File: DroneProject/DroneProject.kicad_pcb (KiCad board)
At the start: 4 copper layers, 50 x 100 mm, 106 parts, among them J21 Battery, J22 Debug, J23 UART, Q21 IRLML5203, SW1 PTS815 SJM 250 SMTR LFS, U31 AP63205WU, U32 TLV75533PDBV, U41 STM32F410RBT6, U61 LSM6DSOTR, U62 TMAG5273C1QDBVR, U63 INA181A1IDBVR, U64 M24C02-WMN6TP, Y41 LFXTAL003151

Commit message: Finished initial PCB layout.  However decided to go ahead and add the motor drivers for the first prototype anyways.  Re-did the reverse-polarity detection to use an NMOS instead of a PMOS.  Added sheets for each motor, still need to decide on parts.
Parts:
- added TP715: PWM2, Library:Testpoint 1.6mm x 0.8mm, F.Cu at (340.9, 72.7)
- added TP716: PWM3, Library:Testpoint 1.6mm x 0.8mm, F.Cu at (340.9, 74.5)
- added TP717: PWM4, Library:Testpoint 1.6mm x 0.8mm, F.Cu at (340.9, 76.3)
- C35, C36, C37, C38, C49, C51, C52, C53, C54, C61, C62, C63, C64, FB41, FB51, FB61, R21, R22, R41, R43, R44, R45, R46, R47, R48, R49, R51, R52, R53, R54, R61, R62, R63: moved to B.Cu
- moved R31 267.4 mm to (137.6, 59.8), turned to 90 degrees
- moved SW31 255.8 mm to (140.9, 64.0), turned to -90 degrees
- moved C39 254.5 mm to (136.4, 59.8), turned to 90 degrees
- moved C62 246.2 mm to (143.6, 111.3), turned to -90 degrees
- moved C610 245.9 mm to (137.5, 142.6), turned to -90 degrees
- moved R63 243.1 mm to (146.0, 109.3)
- moved C64 242.9 mm to (150.2, 104.3), turned to 90 degrees
- moved R62 242.8 mm to (146.0, 108.3)
- moved R61 238.9 mm to (150.2, 106.2), turned to 90 degrees
- moved U61 237.2 mm to (150.0, 108.6)
- moved C66 235.6 mm to (160.1, 101.3), turned to 180 degrees
- moved U63 234.8 mm to (142.3, 139.0), turned to -90 degrees
- moved FB61 233.4 mm to (147.3, 112.0), turned to 90 degrees
- moved C35 231.9 mm to (153.5, 121.2), turned to -90 degrees
- moved R64 231.5 mm to (158.3, 111.6), turned to 90 degrees
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- renumbered SW1 to SW31
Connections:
- net ISEN- renamed GND
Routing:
- net GND: track 0.00 -> 97.4 mm, vias 0 -> 33
- net NRST: track 0.00 -> 88.8 mm, vias 0 -> 4
- net +5V: track 0.00 -> 88.1 mm, vias 0 -> 5
- net +3.3V: track 0.00 -> 79.8 mm, vias 0 -> 13
- net SWO: track 0.00 -> 69.0 mm, vias 0 -> 1
- net ISEN_ADC: track 0.00 -> 59.4 mm, vias 0 -> 2
- net SWCLK: track 0.00 -> 57.1 mm, vias 0 -> 2
- net VBAT_TVS: track 0.00 -> 56.2 mm, vias 0 -> 1
- net MAG_INT: track 0.00 -> 51.4 mm, vias 0 -> 2
- net SWDIO: track 0.00 -> 44.9 mm
- net I2C1_SDA: track 0.00 -> 43.1 mm, vias 0 -> 5
- net I2C1_SCL: track 0.00 -> 42.5 mm, vias 0 -> 3
- net UART_RX: track 0.00 -> 40.5 mm, vias 0 -> 1
- net UART_TX: track 0.00 -> 39.4 mm, vias 0 -> 2
- net EEPROM_WC: track 0.00 -> 38.5 mm, vias 0 -> 4
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- added copper zone on In2.Cu, net +3.3V
- added copper zone on In2.Cu, net +5V
- added copper zone on In1.Cu, net GND
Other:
- board text added: "3.3V"
- board text added: "3P3"
- board text added: "5"
- board text added: "5V"
- board text added: "GND"
- board text added: "I2C1_SCL"
- board text added: "I2C1_SDA"
- board text added: "IMU_CSN"
- board text added: "NRST"
- board text added: "PWR_GOOD"
- board text added: "RESET"
- board text added: "RX"
- board text added: "SPI1_MISO"
- board text added: "SPI1_MOSI"
- board text added: "SPI1_SCK"
- board text added: "SPI2_MISO"
- board text added: "SPI2_MOSI"
- board text added: "SPI2_SCK"
- board text added: "STATUS"
- board text added: "SWCLK"
- board text added: "SWDIO"
- board text added: "SWO"
- board text added: "TR_CSN"
- board text added: "TX"

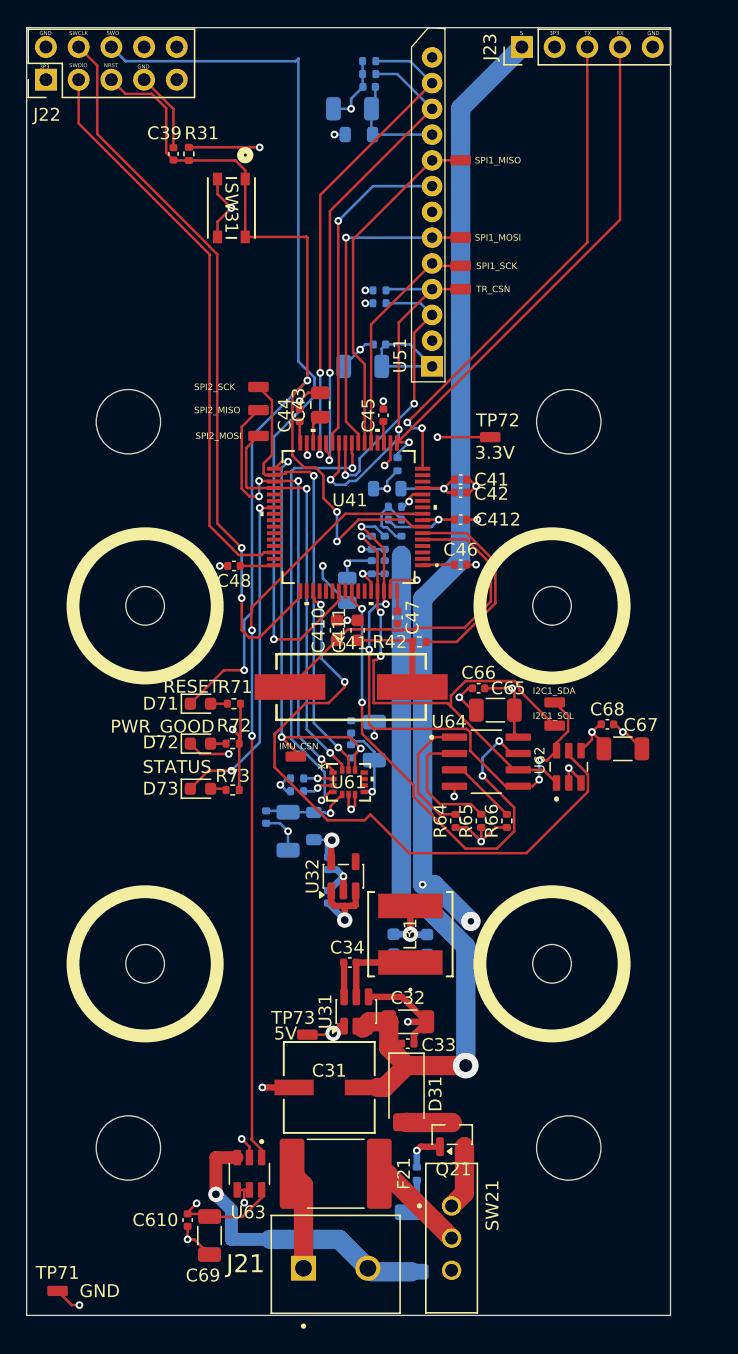
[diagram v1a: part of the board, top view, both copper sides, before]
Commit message: Re-did layout for new power system
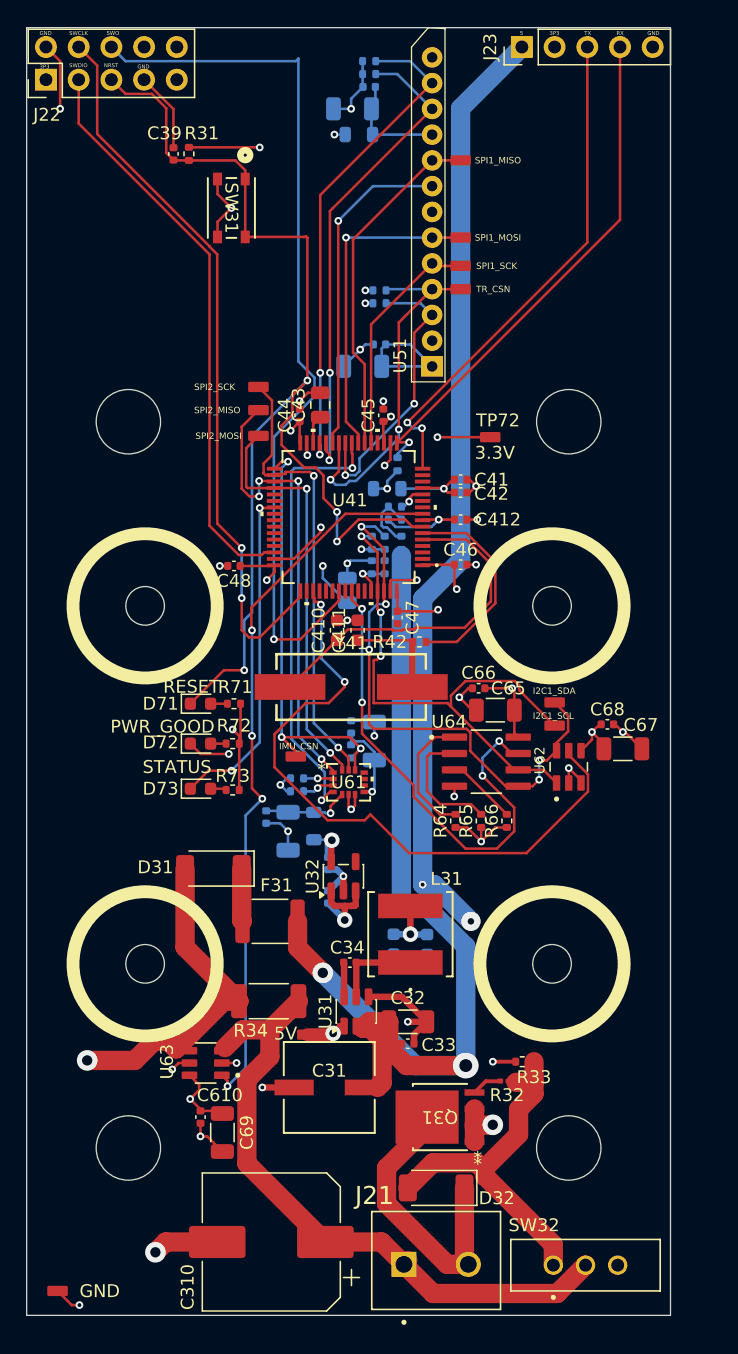
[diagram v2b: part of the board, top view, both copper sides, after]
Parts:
- removed F21: Fuse, Fuse:Fuse_2920_7451Metric
- removed Q21: IRLML5203, Package_TO_SOT_SMD:SOT-23
- removed R21: 100K, Resistor_SMD:R_0402_1005Metric
- removed R22: 5m, Resistor_SMD:R_2010_5025Metric
- removed SW21: ~, Library:SW_EG1218
- added C310: 470uF, Capacitor_SMD:CP_Elec_10x10.5, F.Cu at (144.0, 144.3)
- added D32: SM6F14AY, Diode_SMD:D_SOD-128, F.Cu at (156.8, 140.1)
- added F31: Fuse 1A, Fuse:Fuse_1812_4532Metric, F.Cu at (143.9, 119.4)
- added Q31: RJK0654DPB-00-J5, Library:LFPAK_REN, F.Cu at (157.1, 134.6)
- added R32: 100, Resistor_SMD:R_0201_0603Metric, F.Cu at (162.1, 131.8)
- added R33: 100K, Resistor_SMD:R_0402_1005Metric, F.Cu at (163.5, 130.3)
- added R34: Shunt, Resistor_SMD:R_2010_5025Metric, F.Cu at (143.8, 125.6)
- added SW32: ~, Library:SW_EG1218, F.Cu at (168.4, 146.1)
- moved D31 23.0 mm to (139.5, 115.3), turned to 180 degrees
- moved U63 9.25 mm to (138.9, 130.4), turned to 180 degrees
- moved C610 8.06 mm to (138.5, 134.6)
- moved C69 8.06 mm to (140.2, 135.8)
- moved J21 7.81 mm to (154.3, 146.0)
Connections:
- D31 pad 1: VBAT_TVS -> Net-(D31-K)
- D31 pad 2: VBAT_PROT -> VDD
- J21 pad 2: ISEN+ -> -BATT
- U63 pad 3: ISEN+ -> +BATT
- U63 pad 4: GND -> VDD
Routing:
- net +BATT: track 7.71 -> 50.1 mm
- net /Power/VBAT_SW: track 0.00 -> 28.4 mm
- net VDD: track 0.00 -> 26.2 mm, vias 0 -> 1
- net ISEN+: track 23.5 -> 0.00 mm, vias 1 -> 0
- net -BATT: track 0.00 -> 23.3 mm
- net VBAT_TVS: track 56.2 -> 77.8 mm, vias 1 -> 2
- net GND: track 97.4 -> 114.8 mm, vias 33 -> 38
- net /Connectors/VBAT_FUSE: track 7.68 -> 0.00 mm
- net +3.3V: track 79.8 -> 85.5 mm, vias 13 -> 18
- net /Connectors/VBAT_SW: track 5.01 -> 0.00 mm
- net Net-(D31-K): track 0.00 -> 4.13 mm
- net VBAT_PROT: track 3.56 -> 0.00 mm
- net ISEN_ADC: track 59.4 -> 56.0 mm, vias 2 -> 4
- net /Connectors/VBAT_MOS_GATE: track 3.21 -> 0.00 mm, vias 1 -> 0
- net /Power/VBAT_SW_R: track 0.00 -> 2.28 mm
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- added copper zone on In2.Cu, net VDD

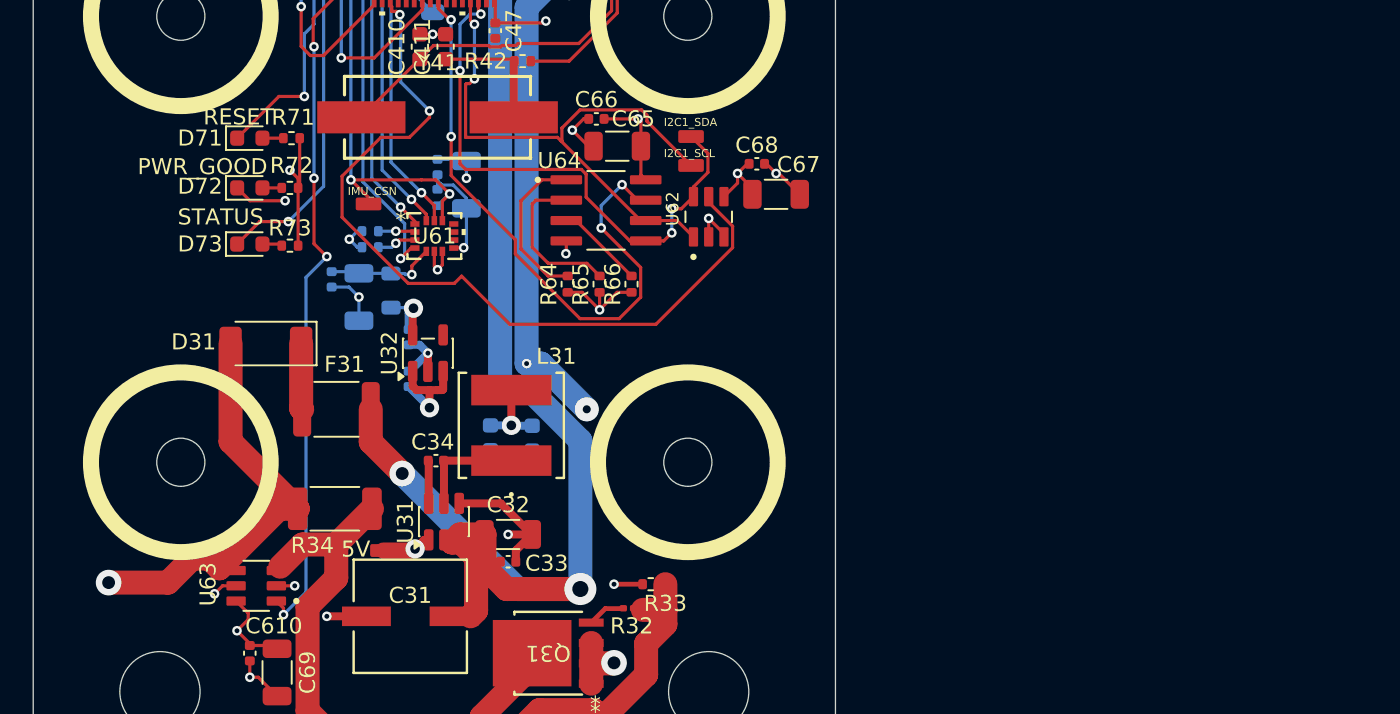
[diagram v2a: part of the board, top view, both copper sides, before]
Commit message: Added a second MCU for motor control.  Removed 5V rail.  Added COM switching for SWD and UART external headers
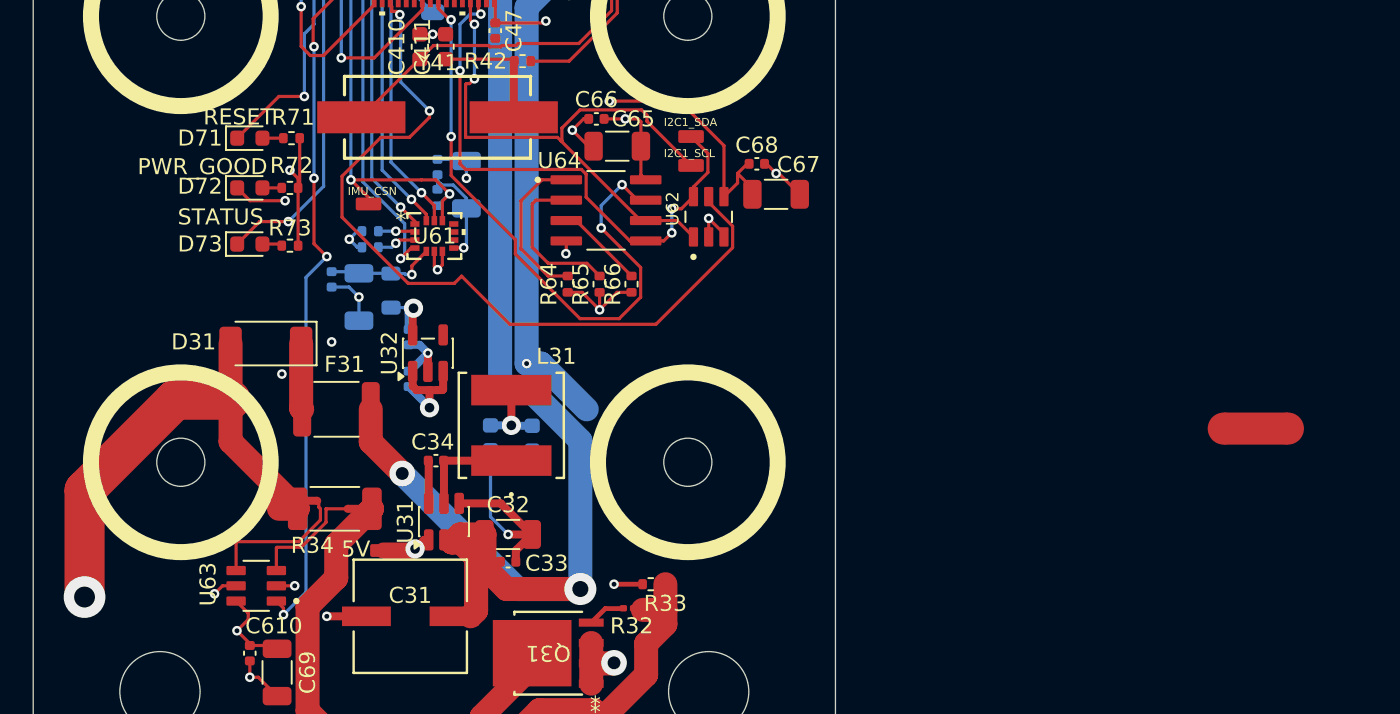
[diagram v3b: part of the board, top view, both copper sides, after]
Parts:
- added NT31: NetTie_2, NetTie:NetTie-2_SMD_Pad0.5mm, F.Cu at (145.1, 125.6)
- added NT32: NetTie_2, NetTie:NetTie-2_SMD_Pad0.5mm, F.Cu at (142.2, 125.1)
- added NT33: NetTie_2, NetTie:NetTie-2_SMD_Pad2.0mm, F.Cu at (201.2, 120.6)
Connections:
- U63 pad 3: +BATT -> ISENSE+
- U63 pad 4: VDD -> ISENSE-
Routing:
- net +3.3V: track 85.5 -> 97.0 mm, vias 18 -> 19
- net ISENSE-: track 0.00 -> 8.86 mm
- net GND: track 114.8 -> 123.3 mm, vias 38 -> 39
- net ISENSE+: track 0.00 -> 7.36 mm
- net VDD: track 26.2 -> 31.3 mm
- net +BATT: track 50.1 -> 46.4 mm
- net +5V: vias 5 -> 4

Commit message: Finished most of routing for motor controls, however likely going to revert back and make separate ESC boards for motor control as I think that would honestly be more efficient from both a cost and debug complexity standpoint.
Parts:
- removed C310: 470uF, Capacitor_SMD:CP_Elec_10x10.5
- removed C39: 0.1uF, Capacitor_SMD:C_0402_1005Metric
- removed C410, C411: 27pF, Capacitor_SMD:C_0603_1608Metric
- removed R42: 0, Resistor_SMD:R_0402_1005Metric
- removed TP714: PWM1, Library:Testpoint 1.6mm x 0.8mm
- removed TP715: PWM2, Library:Testpoint 1.6mm x 0.8mm
- removed TP716: PWM3, Library:Testpoint 1.6mm x 0.8mm
- removed TP717: PWM4, Library:Testpoint 1.6mm x 0.8mm
- removed TP73: POS5, Library:Testpoint 1.6mm x 0.8mm
- removed U32: TLV75533PDBV, Package_TO_SOT_SMD:SOT-23-5
- removed Y41: LFXTAL003151, Library:WE-XTAL_HC49_4HSMX
- added C101: 10uF, Capacitor_SMD:C_1206_3216Metric, F.Cu at (130.5, 114.5)
- added C1010: 1uF, Capacitor_SMD:C_0603_1608Metric, F.Cu at (109.3, 133.6)
- added C1011: 0.1uF, Capacitor_SMD:C_0402_1005Metric, B.Cu at (127.1, 121.6)
- added C1012: 1uF, Capacitor_SMD:C_0603_1608Metric, F.Cu at (112.4, 126.1)
- added C1013: 1uF, Capacitor_SMD:C_0603_1608Metric, F.Cu at (109.3, 126.1)
- added C1014: 1uF, Capacitor_SMD:C_0603_1608Metric, F.Cu at (112.3, 118.5)
- added C1015: 1uF, Capacitor_SMD:C_0603_1608Metric, F.Cu at (109.3, 118.5)
- added C102: 0.1uF, Capacitor_SMD:C_0402_1005Metric, F.Cu at (128.8, 115.8)
- added C103: 1uF, Capacitor_SMD:C_0402_1005Metric, F.Cu at (127.8, 115.8)
- added C104: 47nF, Capacitor_SMD:C_0402_1005Metric, F.Cu at (126.4, 113.4)
- added C105: 1uF, Capacitor_SMD:C_0402_1005Metric, B.Cu at (118.4, 115.5)
- added C106: 440uF, Capacitor_THT:CP_Radial_D10.0mm_P5.00mm, F.Cu at (115.6, 142.0)
- added C108: 0.1uF, Capacitor_SMD:C_0402_1005Metric, B.Cu at (127.1, 129.1)
- added C109: 1uF, Capacitor_SMD:C_0603_1608Metric, F.Cu at (112.4, 133.6)
- added C111: 10uF, Capacitor_SMD:C_1206_3216Metric, F.Cu at (175.5, 100.3)
- added C1110: 1uF, Capacitor_SMD:C_0603_1608Metric, F.Cu at (191.1, 92.7)
- added C1111: 0.1uF, Capacitor_SMD:C_0402_1005Metric, B.Cu at (173.0, 91.8)
- added C1112: 1uF, Capacitor_SMD:C_0603_1608Metric, F.Cu at (188.4, 85.2)
- added C1113: 1uF, Capacitor_SMD:C_0603_1608Metric, F.Cu at (191.4, 85.2)
- added C1114: 1uF, Capacitor_SMD:C_0603_1608Metric, F.Cu at (188.4, 77.5)
- added C1115: 1uF, Capacitor_SMD:C_0603_1608Metric, F.Cu at (191.4, 77.5)
- added C112: 0.1uF, Capacitor_SMD:C_0402_1005Metric, F.Cu at (177.2, 99.0)
- added C113: 1uF, Capacitor_SMD:C_0402_1005Metric, F.Cu at (178.2, 99.0)
- added C114: 47nF, Capacitor_SMD:C_0402_1005Metric, F.Cu at (177.7, 101.5)
- added C115: 1uF, Capacitor_SMD:C_0402_1005Metric, B.Cu at (187.6, 99.7)
- added C116: 440uF, Capacitor_THT:CP_Radial_D10.0mm_P5.00mm, F.Cu at (197.4, 102.0)
- added C118: 0.1uF, Capacitor_SMD:C_0402_1005Metric, B.Cu at (172.8, 84.3)
- added C119: 1uF, Capacitor_SMD:C_0603_1608Metric, F.Cu at (188.0, 92.7)
- added C121: 10uF, Capacitor_SMD:C_1206_3216Metric, F.Cu at (112.0, 96.8)
- added C1210: 1uF, Capacitor_SMD:C_0603_1608Metric, F.Cu at (108.5, 92.7)
- added C1211: 0.1uF, Capacitor_SMD:C_0402_1005Metric, B.Cu at (127.0, 77.9)
- added C1212: 1uF, Capacitor_SMD:C_0603_1608Metric, F.Cu at (111.6, 85.1)
- added C1213: 1uF, Capacitor_SMD:C_0603_1608Metric, F.Cu at (108.5, 85.1)
- added C1214: 1uF, Capacitor_SMD:C_0603_1608Metric, F.Cu at (111.7, 77.5)
- added C1215: 1uF, Capacitor_SMD:C_0603_1608Metric, F.Cu at (108.7, 77.5)
- added C122: 0.1uF, Capacitor_SMD:C_0402_1005Metric, F.Cu at (113.7, 98.1)
- added C123: 1uF, Capacitor_SMD:C_0402_1005Metric, F.Cu at (114.7, 99.1)
- added C124: 47nF, Capacitor_SMD:C_0402_1005Metric, F.Cu at (114.2, 101.4)
- added C125: 1uF, Capacitor_SMD:C_0402_1005Metric, B.Cu at (123.3, 99.7)
- added C126: 440uF, Capacitor_THT:CP_Radial_D10.0mm_P5.00mm, F.Cu at (102.6, 102.0)
- added C128: 0.1uF, Capacitor_SMD:C_0402_1005Metric, B.Cu at (127.1, 85.5)
- added C129: 1uF, Capacitor_SMD:C_0603_1608Metric, F.Cu at (111.5, 92.7)
- added C131: 0.1uF, Capacitor_SMD:C_0402_1005Metric, F.Cu at (139.2, 64.0)
- added C133: 0.1uF, Capacitor_SMD:C_0402_1005Metric, F.Cu at (130.6, 64.0)
- added C134: 0.1uF, Capacitor_SMD:C_0402_1005Metric, F.Cu at (180.6, 58.3)
- added C81: 4.7uF, Capacitor_SMD:C_0805_2012Metric, B.Cu at (161.3, 109.0)
- added C810: 1nf, Capacitor_SMD:C_0402_1005Metric, B.Cu at (140.0, 101.8)
- added C811: 1nf, Capacitor_SMD:C_0402_1005Metric, B.Cu at (135.0, 102.9)
- added C812: 1nf, Capacitor_SMD:C_0402_1005Metric, B.Cu at (135.0, 100.9)
- added C813: 1uF, Capacitor_SMD:C_0402_1005Metric, B.Cu at (149.1, 92.5)
- added C814: 0.1uF, Capacitor_SMD:C_0402_1005Metric, B.Cu at (150.1, 92.5)
- added C815: 1nf, Capacitor_SMD:C_0402_1005Metric, B.Cu at (145.6, 89.7)
- added C816: 1nf, Capacitor_SMD:C_0402_1005Metric, B.Cu at (147.6, 89.7)
- added C817: 1nf, Capacitor_SMD:C_0402_1005Metric, B.Cu at (149.6, 89.8)
- added C818: 1nf, Capacitor_SMD:C_0402_1005Metric, B.Cu at (151.6, 89.8)
- added C82: 0.1uF, Capacitor_SMD:C_0402_1005Metric, B.Cu at (156.8, 96.1)
- added C83: 0.1uF, Capacitor_SMD:C_0402_1005Metric, B.Cu at (160.5, 107.5)
- added C84: 0.1uF, Capacitor_SMD:C_0402_1005Metric, B.Cu at (140.1, 108.3)
- added C85: 0.1uF, Capacitor_SMD:C_0402_1005Metric, B.Cu at (146.6, 114.1)
- added C86: 0.1uF, Capacitor_SMD:C_0402_1005Metric, B.Cu at (140.1, 99.2)
- added C87: 1uF, Capacitor_SMD:C_0402_1005Metric, B.Cu at (154.4, 95.0)
- added C88: 10nF, Capacitor_SMD:C_0402_1005Metric, B.Cu at (155.4, 95.0)
- added C89: 1nf, Capacitor_SMD:C_0402_1005Metric, B.Cu at (140.0, 105.0)
- added C91: 10uF, Capacitor_SMD:C_1206_3216Metric, F.Cu at (183.3, 117.1)
- added C910: 1uF, Capacitor_SMD:C_0603_1608Metric, F.Cu at (191.9, 133.8)
- added C911: 0.1uF, Capacitor_SMD:C_0402_1005Metric, B.Cu at (172.8, 129.2)
- added C912: 1uF, Capacitor_SMD:C_0603_1608Metric, F.Cu at (188.8, 126.4)
- added C913: 1uF, Capacitor_SMD:C_0603_1608Metric, F.Cu at (191.9, 126.4)
- added C914: 1uF, Capacitor_SMD:C_0603_1608Metric, F.Cu at (188.9, 118.4)
- added C915: 1uF, Capacitor_SMD:C_0603_1608Metric, F.Cu at (191.9, 118.4)
- added C92: 0.1uF, Capacitor_SMD:C_0402_1005Metric, F.Cu at (181.6, 115.8)
- added C93: 1uF, Capacitor_SMD:C_0402_1005Metric, F.Cu at (180.6, 115.8)
- added C94: 47nF, Capacitor_SMD:C_0402_1005Metric, F.Cu at (179.2, 113.4)
- added C95: 1uF, Capacitor_SMD:C_0402_1005Metric, B.Cu at (171.2, 114.5)
- added C96: 440uF, Capacitor_THT:CP_Radial_D10.0mm_P5.00mm, F.Cu at (184.4, 142.0)
- added C98: 0.1uF, Capacitor_SMD:C_0402_1005Metric, B.Cu at (172.7, 134.5)
- added C99: 1uF, Capacitor_SMD:C_0603_1608Metric, F.Cu at (188.8, 133.8)
- added D131: C1, LED_SMD:LED_0603_1608Metric, F.Cu at (169.6, 62.8)
- added D132: C0, LED_SMD:LED_0603_1608Metric, F.Cu at (167.9, 62.8)
- added FB81: FerriteBead, Inductor_SMD:L_0805_2012Metric, B.Cu at (152.3, 94.2)
- added J24: Screw_Terminal_01x03, Library:CUI_TB005_-762-03BE, F.Cu at (198.4, 130.2)
- added J25: Screw_Terminal_01x03, Library:CUI_TB005_-762-03BE, F.Cu at (101.7, 114.9)
- added J26: Screw_Terminal_01x03, Library:CUI_TB005_-762-03BE, F.Cu at (198.4, 89.1)
- added J27: Screw_Terminal_01x03, Library:CUI_TB005_-762-03BE, F.Cu at (101.6, 73.9)
- added NT10: NetTie_2, NetTie:NetTie-2_SMD_Pad0.5mm, B.Cu at (123.5, 88.2)
- added NT101: NetTie_2, NetTie:NetTie-2_SMD_Pad0.5mm, B.Cu at (118.9, 130.9)
- added NT102: NetTie_2, NetTie:NetTie-2_SMD_Pad0.5mm, B.Cu at (118.9, 123.4)
- added NT111: NetTie_2, NetTie:NetTie-2_SMD_Pad0.5mm, B.Cu at (181.2, 90.0)
- added NT112: NetTie_2, NetTie:NetTie-2_SMD_Pad0.5mm, B.Cu at (181.0, 82.5)
- added NT12: NetTie_2, NetTie:NetTie-2_SMD_Pad0.5mm, B.Cu at (123.5, 80.6)
- added NT121: NetTie_2, NetTie:NetTie-2_SMD_Pad0.5mm, B.Cu at (119.0, 88.2)
- added NT122: NetTie_2, NetTie:NetTie-2_SMD_Pad0.5mm, B.Cu at (119.0, 80.6)
- added NT2: NetTie_2, NetTie:NetTie-2_SMD_Pad0.5mm, B.Cu at (123.6, 130.9)
- added NT4: NetTie_2, NetTie:NetTie-2_SMD_Pad0.5mm, B.Cu at (123.6, 123.4)
- added NT6: NetTie_2, NetTie:NetTie-2_SMD_Pad0.5mm, B.Cu at (176.5, 90.0)
- added NT8: NetTie_2, NetTie:NetTie-2_SMD_Pad0.5mm, B.Cu at (176.3, 82.5)
- added NT91: NetTie_2, NetTie:NetTie-2_SMD_Pad0.5mm, B.Cu at (181.1, 132.4)
- added NT92: NetTie_2, NetTie:NetTie-2_SMD_Pad0.5mm, B.Cu at (176.4, 132.4)
- added NT93: NetTie_2, NetTie:NetTie-2_SMD_Pad0.5mm, B.Cu at (180.9, 127.0)
- added NT94: NetTie_2, NetTie:NetTie-2_SMD_Pad0.5mm, B.Cu at (176.4, 127.0)
- added Q101: CSD17577Q5A, Package_TO_SOT_SMD:TDSON-8-1, F.Cu at (110.3, 130.0)
- added Q102: CSD17577Q5A, Package_TO_SOT_SMD:TDSON-8-1, B.Cu at (113.8, 130.0)
- added Q103: CSD17577Q5A, Package_TO_SOT_SMD:TDSON-8-1, F.Cu at (110.3, 122.5)
- added Q104: CSD17577Q5A, Package_TO_SOT_SMD:TDSON-8-1, B.Cu at (113.8, 122.5)
- added Q105: CSD17577Q5A, Package_TO_SOT_SMD:TDSON-8-1, F.Cu at (110.3, 114.8)
- added Q106: CSD17577Q5A, Package_TO_SOT_SMD:TDSON-8-1, B.Cu at (113.8, 114.8)
- added Q111: CSD17577Q5A, Package_TO_SOT_SMD:TDSON-8-1, F.Cu at (189.8, 89.1)
- added Q112: CSD17577Q5A, Package_TO_SOT_SMD:TDSON-8-1, B.Cu at (186.3, 89.1)
- added Q113: CSD17577Q5A, Package_TO_SOT_SMD:TDSON-8-1, F.Cu at (189.8, 81.5)
- added Q114: CSD17577Q5A, Package_TO_SOT_SMD:TDSON-8-1, B.Cu at (186.2, 81.5)
- added Q115: CSD17577Q5A, Package_TO_SOT_SMD:TDSON-8-1, F.Cu at (189.8, 73.9)
- added Q116: CSD17577Q5A, Package_TO_SOT_SMD:TDSON-8-1, B.Cu at (186.3, 73.9)
- added Q121: CSD17577Q5A, Package_TO_SOT_SMD:TDSON-8-1, F.Cu at (110.2, 89.1)
- added Q122: CSD17577Q5A, Package_TO_SOT_SMD:TDSON-8-1, B.Cu at (113.8, 89.1)
- added Q123: CSD17577Q5A, Package_TO_SOT_SMD:TDSON-8-1, F.Cu at (110.2, 81.5)
- added Q124: CSD17577Q5A, Package_TO_SOT_SMD:TDSON-8-1, B.Cu at (113.7, 81.5)
- added Q125: CSD17577Q5A, Package_TO_SOT_SMD:TDSON-8-1, F.Cu at (110.2, 73.8)
- added Q126: CSD17577Q5A, Package_TO_SOT_SMD:TDSON-8-1, B.Cu at (113.7, 73.8)
- added Q91: CSD17577Q5A, Package_TO_SOT_SMD:TDSON-8-1, F.Cu at (189.8, 130.2)
- added Q92: CSD17577Q5A, Package_TO_SOT_SMD:TDSON-8-1, B.Cu at (186.2, 130.2)
- added Q93: CSD17577Q5A, Package_TO_SOT_SMD:TDSON-8-1, F.Cu at (189.8, 122.7)
- added Q94: CSD17577Q5A, Package_TO_SOT_SMD:TDSON-8-1, B.Cu at (186.2, 122.7)
- added Q95: CSD17577Q5A, Package_TO_SOT_SMD:TDSON-8-1, F.Cu at (189.8, 114.9)
- added Q96: CSD17577Q5A, Package_TO_SOT_SMD:TDSON-8-1, B.Cu at (186.2, 114.9)
- added R101: 10K, Resistor_SMD:R_0402_1005Metric, B.Cu at (118.4, 116.5)
- added R102: 10K, Resistor_SMD:R_0402_1005Metric, B.Cu at (122.1, 112.1)
- added R103: 10K, Resistor_SMD:R_0402_1005Metric, B.Cu at (123.1, 112.1)
- added R104: 10K, Resistor_SMD:R_0402_1005Metric, B.Cu at (124.1, 112.1)
- added R105: 10K, Resistor_SMD:R_0402_1005Metric, B.Cu at (118.4, 119.5)
- added R106: 33, Resistor_SMD:R_0402_1005Metric, B.Cu at (118.4, 118.5)
- added R107: 10K, Resistor_SMD:R_0402_1005Metric, B.Cu at (118.4, 117.5)
- added R108: CSS2H-2512K-2L00J, Resistor_SMD:R_2512_6332Metric, B.Cu at (121.2, 130.9)
- added R109: CSS2H-2512K-2L00J, Resistor_SMD:R_2512_6332Metric, B.Cu at (121.2, 123.4)
- added R111: 10K, Resistor_SMD:R_0402_1005Metric, B.Cu at (187.5, 98.7)
- added R112: 10K, Resistor_SMD:R_0402_1005Metric, B.Cu at (183.0, 103.9)
- added R113: 10K, Resistor_SMD:R_0402_1005Metric, B.Cu at (182.0, 103.9)
- added R114: 10K, Resistor_SMD:R_0402_1005Metric, B.Cu at (181.0, 103.9)
- added R115: 10K, Resistor_SMD:R_0402_1005Metric, B.Cu at (187.5, 95.7)
- added R116: 33, Resistor_SMD:R_0402_1005Metric, B.Cu at (187.5, 96.7)
- added R117: 10K, Resistor_SMD:R_0402_1005Metric, B.Cu at (187.5, 97.7)
- added R118: CSS2H-2512K-2L00J, Resistor_SMD:R_2512_6332Metric, B.Cu at (178.9, 90.0)
- added R119: CSS2H-2512K-2L00J, Resistor_SMD:R_2512_6332Metric, B.Cu at (178.7, 82.5)
- added R121: 10K, Resistor_SMD:R_0402_1005Metric, B.Cu at (123.3, 98.7)
- added R122: 10K, Resistor_SMD:R_0402_1005Metric, B.Cu at (119.6, 103.9)
- added R123: 10K, Resistor_SMD:R_0402_1005Metric, B.Cu at (118.6, 103.9)
- added R124: 10K, Resistor_SMD:R_0402_1005Metric, B.Cu at (117.6, 103.9)
- added R125: 10K, Resistor_SMD:R_0402_1005Metric, B.Cu at (123.3, 95.7)
- added R126: 33, Resistor_SMD:R_0402_1005Metric, B.Cu at (123.3, 96.7)
- added R127: 10K, Resistor_SMD:R_0402_1005Metric, B.Cu at (123.3, 97.7)
- added R128: CSS2H-2512K-2L00J, Resistor_SMD:R_2512_6332Metric, B.Cu at (121.2, 88.2)
- added R129: CSS2H-2512K-2L00J, Resistor_SMD:R_2512_6332Metric, B.Cu at (121.2, 80.6)
- added R131: 10K, Resistor_SMD:R_0402_1005Metric, F.Cu at (161.6, 53.0)
- added R132: 1K, Resistor_SMD:R_0402_1005Metric, F.Cu at (169.3, 60.1)
- added R133: 1K, Resistor_SMD:R_0402_1005Metric, F.Cu at (168.2, 60.1)
- added R134: 10K, Resistor_SMD:R_0402_1005Metric, F.Cu at (141.0, 54.0)
- added R135: 10K, Resistor_SMD:R_0402_1005Metric, F.Cu at (141.0, 57.7)
- added R410: 33, Resistor_SMD:R_0402_1005Metric, F.Cu at (158.5, 86.1)
- added R411: 33, Resistor_SMD:R_0402_1005Metric, F.Cu at (151.7, 81.5)
- added R412: 33, Resistor_SMD:R_0402_1005Metric, F.Cu at (150.7, 81.5)
- added R413: 10K, Resistor_SMD:R_0402_1005Metric, F.Cu at (141.5, 91.4)
- added R414: 33, Resistor_SMD:R_0402_1005Metric, F.Cu at (141.5, 92.8)
- added R415: 33, Resistor_SMD:R_0402_1005Metric, F.Cu at (146.2, 99.3)
- added R416: 33, Resistor_SMD:R_0402_1005Metric, F.Cu at (149.2, 81.5)
- added R417: 33, Resistor_SMD:R_0402_1005Metric, F.Cu at (141.5, 86.4)
- added R418: 33, Resistor_SMD:R_0402_1005Metric, F.Cu at (141.5, 87.4)
- added R419: 33, Resistor_SMD:R_0402_1005Metric, F.Cu at (141.5, 88.4)
- added R420: 33, Resistor_SMD:R_0402_1005Metric, F.Cu at (141.5, 89.4)
- added R421: 10K, Resistor_SMD:R_0402_1005Metric, F.Cu at (149.3, 101.2)
- added R422: 33, Resistor_SMD:R_0402_1005Metric, F.Cu at (148.8, 99.3)
- added R423: 33, Resistor_SMD:R_0402_1005Metric, F.Cu at (155.3, 81.5)
- added R424: 33, Resistor_SMD:R_0402_1005Metric, F.Cu at (141.5, 90.4)
- added R81: 100, Resistor_SMD:R_0402_1005Metric, B.Cu at (140.0, 104.0)
- added R810: 100, Resistor_SMD:R_0402_1005Metric, B.Cu at (148.6, 89.7)
- added R811: 100, Resistor_SMD:R_0402_1005Metric, B.Cu at (146.6, 89.7)
- added R812: 100, Resistor_SMD:R_0402_1005Metric, B.Cu at (150.6, 89.8)
- added R813: 10K, Resistor_SMD:R_0402_1005Metric, B.Cu at (153.8, 116.3)
- added R814: 33, Resistor_SMD:R_0402_1005Metric, B.Cu at (160.5, 105.9)
- added R815: 33, Resistor_SMD:R_0402_1005Metric, B.Cu at (153.8, 114.1)
- added R816: 33, Resistor_SMD:R_0402_1005Metric, B.Cu at (152.8, 114.1)
- added R817: 33, Resistor_SMD:R_0402_1005Metric, B.Cu at (151.8, 114.1)
- added R818: 10K, Resistor_SMD:R_0402_1005Metric, B.Cu at (151.8, 116.5)
- added R819: 10K, Resistor_SMD:R_0402_1005Metric, B.Cu at (150.8, 116.5)
- added R82: 100, Resistor_SMD:R_0402_1005Metric, B.Cu at (140.0, 103.0)
- added R820: 100, Resistor_SMD:R_0402_1005Metric, B.Cu at (152.6, 89.8)
- added R821: 33, Resistor_SMD:R_0402_1005Metric, B.Cu at (150.8, 114.1)
- added R822: 33, Resistor_SMD:R_0402_1005Metric, B.Cu at (149.7, 114.1)
- added R823: 10K, Resistor_SMD:R_0402_1005Metric, B.Cu at (147.6, 114.1)
- added R824: 33, Resistor_SMD:R_0402_1005Metric, B.Cu at (160.6, 100.1)
- added R83: 100, Resistor_SMD:R_0402_1005Metric, B.Cu at (135.0, 103.9)
- added R84: 100, Resistor_SMD:R_0402_1005Metric, B.Cu at (135.0, 101.9)
- added R85: 33, Resistor_SMD:R_0402_1005Metric, B.Cu at (148.2, 95.5)
- added R86: 33, Resistor_SMD:R_0402_1005Metric, B.Cu at (160.5, 103.6)
- added R87: 33, Resistor_SMD:R_0402_1005Metric, B.Cu at (160.5, 102.4)
- added R88: 10K, Resistor_SMD:R_0402_1005Metric, B.Cu at (149.2, 95.5)
- added R89: 33, Resistor_SMD:R_0402_1005Metric, B.Cu at (146.2, 95.5)
- added R91: 10K, Resistor_SMD:R_0402_1005Metric, B.Cu at (171.2, 115.8)
- added R92: 10K, Resistor_SMD:R_0402_1005Metric, B.Cu at (175.2, 112.2)
- added R93: 10K, Resistor_SMD:R_0402_1005Metric, B.Cu at (176.2, 112.2)
- added R94: 10K, Resistor_SMD:R_0402_1005Metric, B.Cu at (177.2, 112.2)
- added R95: 10K, Resistor_SMD:R_0402_1005Metric, B.Cu at (171.2, 120.4)
- added R96: 33, Resistor_SMD:R_0402_1005Metric, B.Cu at (171.2, 119.0)
- added R97: 10K, Resistor_SMD:R_0402_1005Metric, B.Cu at (171.2, 117.5)
- added R98: CSS2H-2512K-2L00J, Resistor_SMD:R_2512_6332Metric, B.Cu at (178.8, 132.4)
- added R99: CSS2H-2512K-2L00J, Resistor_SMD:R_2512_6332Metric, B.Cu at (178.7, 127.0)
- added SW131: TS02CBE, Library:SW_TS02_10P16X5P08_CNK, F.Cu at (165.7, 53.0)
- added U101: DRV8320SRTVR, Library:DRV8320SRTVR, B.Cu at (123.5, 117.8)
- added U102: INA180A2, Package_TO_SOT_SMD:SOT-23-5, B.Cu at (127.1, 131.3)
- added U103: INA180A2, Package_TO_SOT_SMD:SOT-23-5, B.Cu at (127.1, 123.8)
- added U111: DRV8320SRTVR, Library:DRV8320SRTVR, B.Cu at (181.7, 97.9)
- added U112: INA180A2, Package_TO_SOT_SMD:SOT-23-5, B.Cu at (173.0, 89.5)
- added U113: INA180A2, Package_TO_SOT_SMD:SOT-23-5, B.Cu at (172.7, 82.0)
- added U121: DRV8320SRTVR, Library:DRV8320SRTVR, B.Cu at (118.3, 97.9)
- added U122: INA180A2, Package_TO_SOT_SMD:SOT-23-5, B.Cu at (127.1, 87.8)
- added U123: INA180A2, Package_TO_SOT_SMD:SOT-23-5, B.Cu at (127.0, 80.2)
- added U131: NC7SZ04P5X, Library:SC-88A-5_1P35X2P2_ONS, F.Cu at (168.2, 57.6)
- added U132: TS3A4751PWR, Library:SOP65P640X120-14N, F.Cu at (136.2, 67.3)
- added U133: SN74LVC1G08DBVR, Library:SOT95P280X145-5N, F.Cu at (137.9, 53.1)
- added U134: TS3A4751PWR, Library:SOP65P640X120-14N, F.Cu at (127.6, 67.3)
- added U135: SN74LVC1G08DBVR, Library:SOT95P280X145-5N, F.Cu at (137.9, 56.7)
- added U136: TS3A4751PWR, Library:SOP65P640X120-14N, F.Cu at (177.6, 61.6)
- added U81: STM32G431RBTx, Package_QFP:LQFP-64_10x10mm_P0.5mm, B.Cu at (150.0, 103.7)
- added U91: DRV8320SRTVR, Library:DRV8320SRTVR, B.Cu at (176.5, 117.8)
- added U92: INA180A2, Package_TO_SOT_SMD:SOT-23-5, B.Cu at (172.8, 132.3)
- added U93: INA180A2, Package_TO_SOT_SMD:SOT-23-5, B.Cu at (172.8, 127.0)
- C35, C36, C49, C51, C52, C53, C54, C61, C62, C63, C64, FB41, FB51, FB61, R41, R43, R44, R45, R46, R47, R48, R49, R51, R52, R53, R54, R61, R62, R63: moved to F.Cu
- C37: value 1uF -> 0.1uF; moved to F.Cu
- C38: value 0.47uF -> 470uF; footprint Capacitor_SMD:C_0402_1005Metric -> Capacitor_SMD:CP_Elec_10x10.5; moved to F.Cu
- TP74: value SPI1_MOSI -> C0_SPI1_MOSI
- TP75: value SPI1_MISO -> C0_SPI1_MISO
- TP76: value SPI1_SCK -> C0_SPI1_SCK
- U31: value AP63205WU -> AP63203WU
- moved TP710 284.3 mm to (396.9, 205.8)
- moved TP79 283.6 mm to (394.3, 211.2)
- moved TP78 281.9 mm to (394.3, 209.4)
- moved TP75 277.6 mm to (391.7, 211.2)
- moved R71 274.0 mm to (391.9, 213.1), turned to 0 degrees
- moved R72 273.7 mm to (391.9, 215.1), turned to 0 degrees
- moved TP74 273.4 mm to (391.7, 209.4)
- moved R73 273.1 mm to (391.9, 217.0), turned to 0 degrees
- moved TP76 272.7 mm to (394.3, 205.8)
- moved TP77 272.7 mm to (394.3, 207.6)
- moved TP711 270.5 mm to (396.9, 207.6)
- moved D71 270.5 mm to (388.4, 206.2)
- moved TP71 270.5 mm to (391.7, 205.8)
- moved D72 270.3 mm to (388.4, 208.8)
- moved D73 270.0 mm to (388.4, 211.3)
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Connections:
- net I2C1_SCL renamed C0_I2C1_SCL
- net I2C1_SDA renamed C0_I2C1_SDA
- net SPI1_MISO renamed C0_SPI1_MISO
- net SPI2_MISO renamed C0_SPI2_MISO
- C35 pad 1: +5V -> +3.3V
- C36 pad 1: +5V -> +3.3V
- C37 pad 1: +5V -> NRST
- C38 pad 1: +3.3V -> +BATT
- J22 pad 5: NRST -> SWD_NRST
- J23 pad 1: +5V -> unconnected-(J23-Pin_1-Pad1)
- L31 pad 2: +5V -> +3.3V
- R43 pad 1: UART_RX -> C0_UART_RX
- TP710 pad 1: SPI2_SCK -> C0_SPI2_SCK
- TP74 pad 1: SPI1_MOSI -> C0_SPI1_MOSI
- TP76 pad 1: SPI1_SCK -> C0_SPI1_SCK
- TP78 pad 1: SPI2_MOSI -> C0_SPI2_MOSI
- U31 pad 1: +5V -> +3.3V
- U41 pad 16: UART_TX -> Net-(U41B-PA2)
- U41 pad 17: UART_RX -> C0_UART_RX
- U41 pad 20: unconnected-(U41B-PA4-Pad20) -> Net-(U41B-PA4)
- U41 pad 21: SPI1_SCK -> Net-(U41B-PA5)
- U41 pad 23: SPI1_MOSI -> Net-(U41B-PA7)
- U41 pad 26: TR_CSN -> Net-(U41B-PB0)
- U41 pad 33: IMU_CSN -> Net-(U41B-PB12)
- U41 pad 34: SPI2_SCK -> Net-(U41B-PB13)
- U41 pad 36: SPI2_MOSI -> Net-(U41B-PB15)
- U41 pad 37: unconnected-(U41B-PC6-Pad37) -> Net-(U41B-PC6)
- U41 pad 41: PWM1 -> unconnected-(U41B-PA8-Pad41)
- U41 pad 42: PWM2 -> unconnected-(U41B-PA9-Pad42)
- U41 pad 43: PWM3 -> Net-(U41B-PA10)
- U41 pad 44: PWM4 -> unconnected-(U41B-PA11-Pad44)
- U41 pad 45: unconnected-(U41B-PA12-Pad45) -> C0_SPI5_MISO
- U41 pad 46: SWDIO -> Net-(U41B-PA13)
- U41 pad 49: SWCLK -> Net-(U41B-PA14)
- U41 pad 5: /MCU/OSC_IN -> unconnected-(U41B-PH0-OSC_IN-Pad5)
- U41 pad 55: SWO -> Net-(U41B-PB3)
- U41 pad 6: /MCU/OSC_OUT -> unconnected-(U41B-PH1-OSC_OUT-Pad6)
- U41 pad 7: NRST -> C0_NRST
- U51 pad 5: SPI1_SCK -> C0_SPI1_SCK
- U51 pad 6: SPI1_MOSI -> C0_SPI1_MOSI
- U61 pad 13: SPI2_SCK -> C0_SPI2_SCK
- U61 pad 14: SPI2_MOSI -> C0_SPI2_MOSI
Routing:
- net GND: track 123.3 -> 263.4 mm, vias 39 -> 81
- net C1_SPI2_MOSI: track 0.00 -> 139.9 mm, vias 0 -> 10
- net C1_SPI2_SCK: track 0.00 -> 138.7 mm, vias 0 -> 10
- net C1_SPI2_MISO: track 0.00 -> 132.9 mm, vias 0 -> 7
- net +3.3V: track 97.0 -> 213.2 mm, vias 19 -> 50
- net GNDPWR: track 0.00 -> 107.3 mm, vias 0 -> 48
- net C1_SWCLK: track 0.00 -> 103.6 mm, vias 0 -> 7
- net MTR3_CURR_A: track 0.00 -> 101.2 mm, vias 0 -> 4
- net C1_SWO: track 0.00 -> 97.9 mm, vias 0 -> 3
- net C1_SWDIO: track 0.00 -> 96.4 mm, vias 0 -> 3
- net /Prog/C0_SEL: track 0.00 -> 91.1 mm, vias 0 -> 4
- net +5V: track 88.1 -> 0.00 mm, vias 4 -> 0
- net /Prog/C1_SEL: track 0.00 -> 78.3 mm, vias 0 -> 7
- net C1_UART_RX: track 0.00 -> 77.8 mm, vias 0 -> 3
- net NRST: track 89.5 -> 15.9 mm, vias 4 -> 0
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- added copper zone on F.Cu, net +BATT
- added copper zone on In1.Cu, net GNDPWR
- added copper zone on B.Cu, net MTR1_A
- added copper zone on F.Cu, net MTR1_A
- added copper zone on B.Cu, net MTR1_B
- added copper zone on F.Cu, net MTR1_B
- added copper zone on B.Cu, net MTR1_C
- added copper zone on F.Cu, net MTR1_C
- added copper zone on B.Cu, net MTR2_A
- added copper zone on F.Cu, net MTR2_A
- added copper zone on B.Cu, net MTR2_B
- added copper zone on F.Cu, net MTR2_B
- added copper zone on B.Cu, net MTR2_C
- added copper zone on F.Cu, net MTR2_C
- added copper zone on B.Cu, net MTR3_A
- added copper zone on F.Cu, net MTR3_A
- added copper zone on B.Cu, net MTR3_B
- added copper zone on F.Cu, net MTR3_B
- added copper zone on B.Cu, net MTR3_C
- added copper zone on F.Cu, net MTR3_C
- added copper zone on B.Cu, net MTR4_A
- added copper zone on F.Cu, net MTR4_A
- added copper zone on B.Cu, net MTR4_B
- added copper zone on F.Cu, net MTR4_B
- added copper zone on B.Cu, net MTR4_C
- added copper zone on F.Cu, net MTR4_C
- added copper zone on F.Cu, net VDD
- removed copper zone on In2.Cu, net +5V
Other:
- board size 50 x 100 mm -> 100 x 100 mm
- board text added: "C0 Active"
- board text added: "C1 Active"
- board text added: "Q31"
- board text added: "SWD_NRST"
- board text added: "UART_RX"
- board text added: "UART_TX"
- board text removed: "3P3"
- board text removed: "5"
- board text removed: "5V"
- board text removed: "I2C1_SCL"
- board text removed: "I2C1_SDA"
- board text removed: "IMU_CSN"
- board text removed: "NRST"
- board text removed: "PWR_GOOD"
- board text removed: "RX"
- board text removed: "SPI1_MISO"
- board text removed: "SPI1_MOSI"
- board text removed: "SPI1_SCK"
- board text removed: "SPI2_MISO"
- board text removed: "SPI2_MOSI"
- board text removed: "SPI2_SCK"
- board text removed: "STATUS"
- board text removed: "TR_CSN"
- board text removed: "TX"
